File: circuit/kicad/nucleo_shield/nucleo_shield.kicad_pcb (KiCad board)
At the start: 2 copper layers, 31 parts, among them J1 USB_B_Micro, J2 Conn_01x03_Pin, J3 Conn_01x04_Pin, J4 Conn_01x04_Pin, J5 Conn_01x03_Pin, J6 Conn_01x03_Pin, SW1 SW_Push, SW2 SW_Push, U1 NUCLEO-F401RE, U2 CH340G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

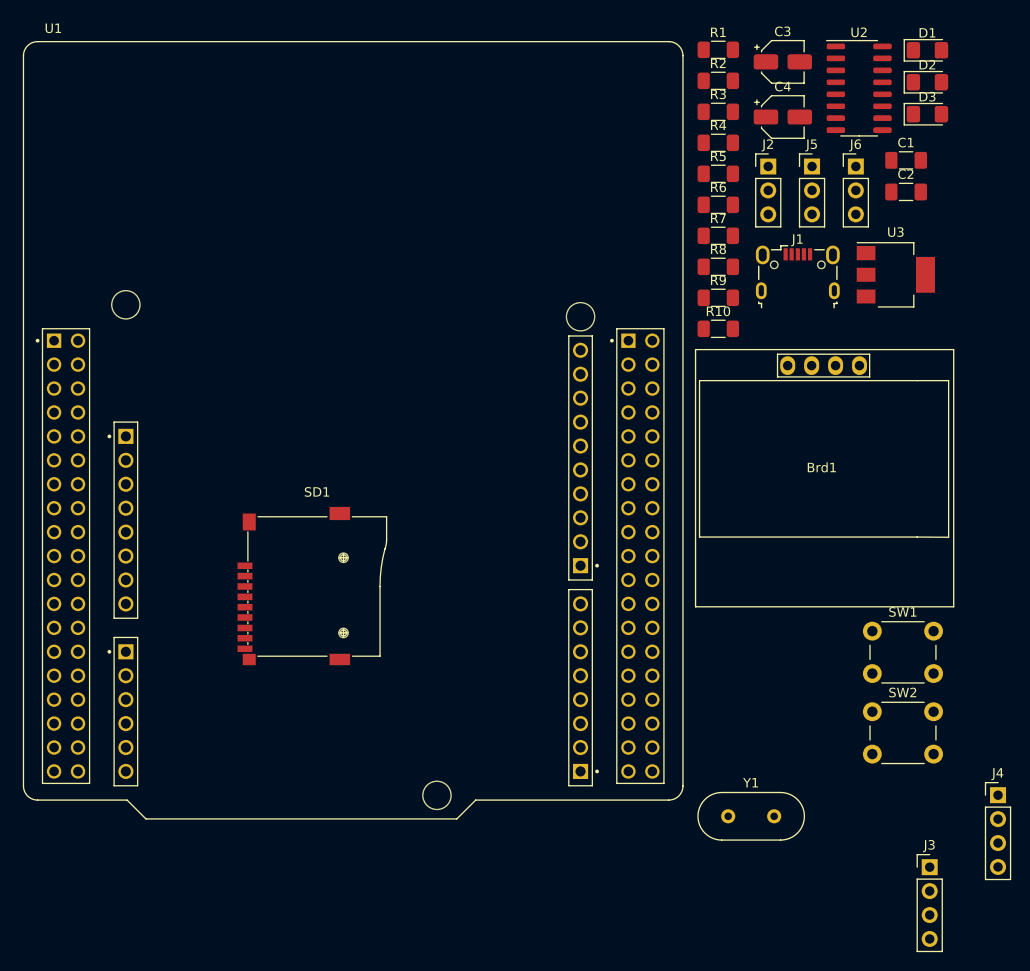
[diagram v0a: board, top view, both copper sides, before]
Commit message: Nucleo Shield
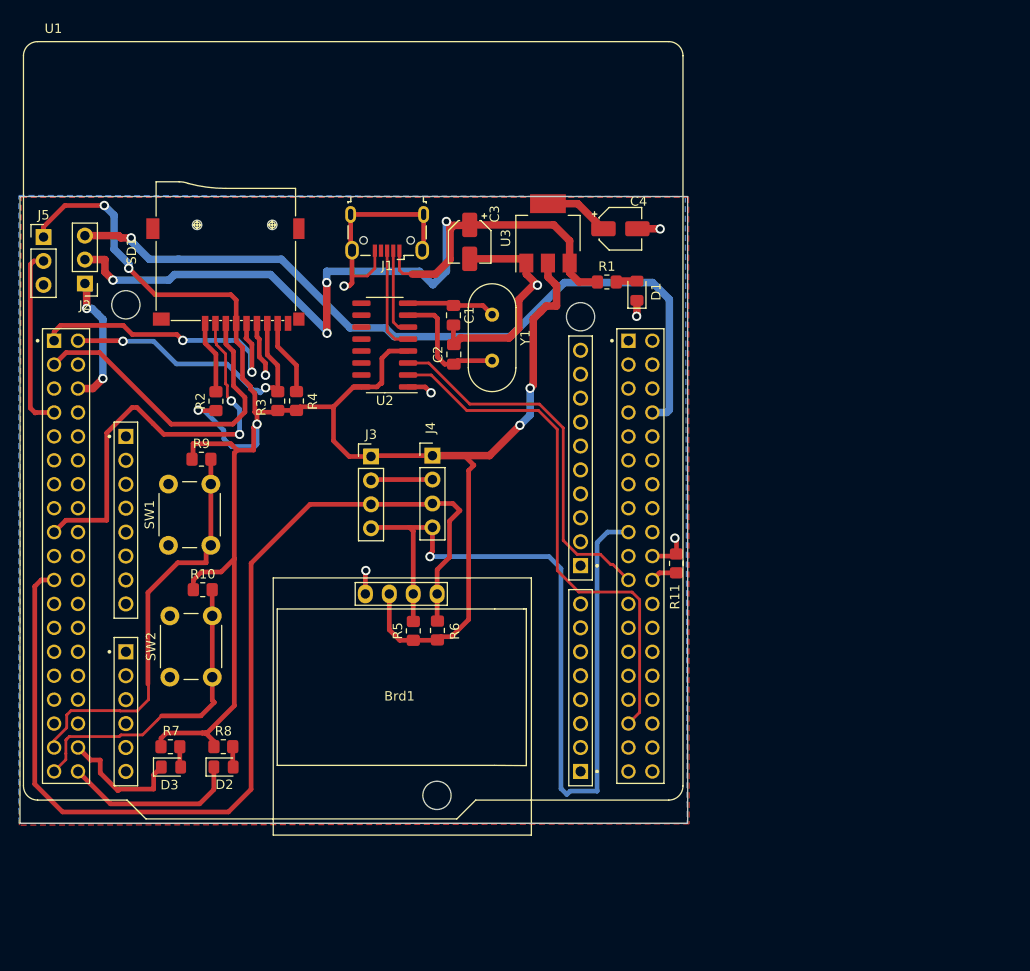
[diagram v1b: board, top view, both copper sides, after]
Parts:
- removed J6: Conn_01x03_Pin, Connector_PinHeader_2.54mm:PinHeader_1x03_P2.54mm_Vertical
- added R11: 0, Resistor_SMD:R_0805_2012Metric_Pad1.20x1.40mm_HandSolder, F.Cu at (240.1, 89.3)
- C1, C2: footprint Capacitor_SMD:C_1206_3216Metric_Pad1.33x1.80mm_HandSolder -> Capacitor_SMD:C_0805_2012Metric_Pad1.18x1.45mm_HandSolder
- D1, D2, D3: footprint LED_SMD:LED_1206_3216Metric_Pad1.42x1.75mm_HandSolder -> LED_SMD:LED_0805_2012Metric_Pad1.15x1.40mm_HandSolder
- R1, R10, R2, R3, R4, R5, R6, R7, R8, R9: footprint Resistor_SMD:R_1206_3216Metric_Pad1.30x1.75mm_HandSolder -> Resistor_SMD:R_0805_2012Metric_Pad1.20x1.40mm_HandSolder
- Y1: footprint Crystal:Crystal_HC49-U_Vertical -> Crystal:Crystal_HC49-4H_Vertical
- moved D3 106.1 mm to (186.4, 111.0)
- moved D2 104.2 mm to (192.0, 111.0)
- moved J5 81.9 mm to (172.9, 54.7)
- moved R7 79.5 mm to (186.4, 108.8)
- moved SW1 75.3 mm to (186.2, 87.4), turned to 90 degrees
- moved SW2 74.7 mm to (186.3, 101.4), turned to 90 degrees
- moved J3 73.6 mm to (207.7, 78.0)
- moved J2 73.6 mm to (177.3, 59.6), turned to 180 degrees
- moved R8 73.2 mm to (192.0, 108.8)
- moved J4 70.0 mm to (214.2, 77.9)
- moved R2 63.2 mm to (191.2, 72.1), turned to 90 degrees
- moved R10 61.3 mm to (189.8, 92.1)
- moved Y1 58.8 mm to (220.5, 63.0), turned to -90 degrees
- moved R5 58.3 mm to (212.2, 96.5), turned to 90 degrees
- moved R9 57.5 mm to (189.7, 78.3)
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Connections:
- R10 pad 2: BTN_A -> BTN_B
- SW2 pad 2: BTN_A -> BTN_B
- U1 pad CN7_14: NRST -> unconnected-(U1A-RESET_S1-PadCN7_14)
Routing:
- net +3V3: track 0.00 -> 220.6 mm, vias 0 -> 6
- net I2C_SDA: track 0.00 -> 110.3 mm
- net I2C_SCL: track 0.00 -> 92.1 mm, vias 0 -> 1
- net VBUS: track 0.00 -> 89.0 mm, vias 0 -> 4
- net +5VD: track 0.00 -> 83.4 mm, vias 0 -> 1
- net GND: track 0.00 -> 75.1 mm, vias 0 -> 8
- net UART_RX: track 0.00 -> 56.9 mm
- net MMC_NSS: track 0.00 -> 44.6 mm, vias 0 -> 2
- net BTN_A: track 0.00 -> 43.5 mm
- net UART_TX: track 0.00 -> 39.9 mm
- net MMC_MOSI: track 0.00 -> 34.7 mm
- net BTN_B: track 0.00 -> 33.3 mm
- net MMC_MISO: track 0.00 -> 31.8 mm, vias 0 -> 2
- net MMC_SCK: track 0.00 -> 31.0 mm, vias 0 -> 2
- net BOOT0: track 0.00 -> 19.5 mm
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- added copper zone on F.Cu, net (none)
- added copper zone on B.Cu, net GND
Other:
- board outline added: 70.9 x 66.5 mm
